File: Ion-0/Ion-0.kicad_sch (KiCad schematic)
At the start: 15 parts, among them J1 Beaglebone-green-P9, J2 Beaglebone-green-P8, J3 Conn_02x06_Odd_Even, J4 Conn_02x06_Odd_Even, J5 Conn_02x06_Odd_Even

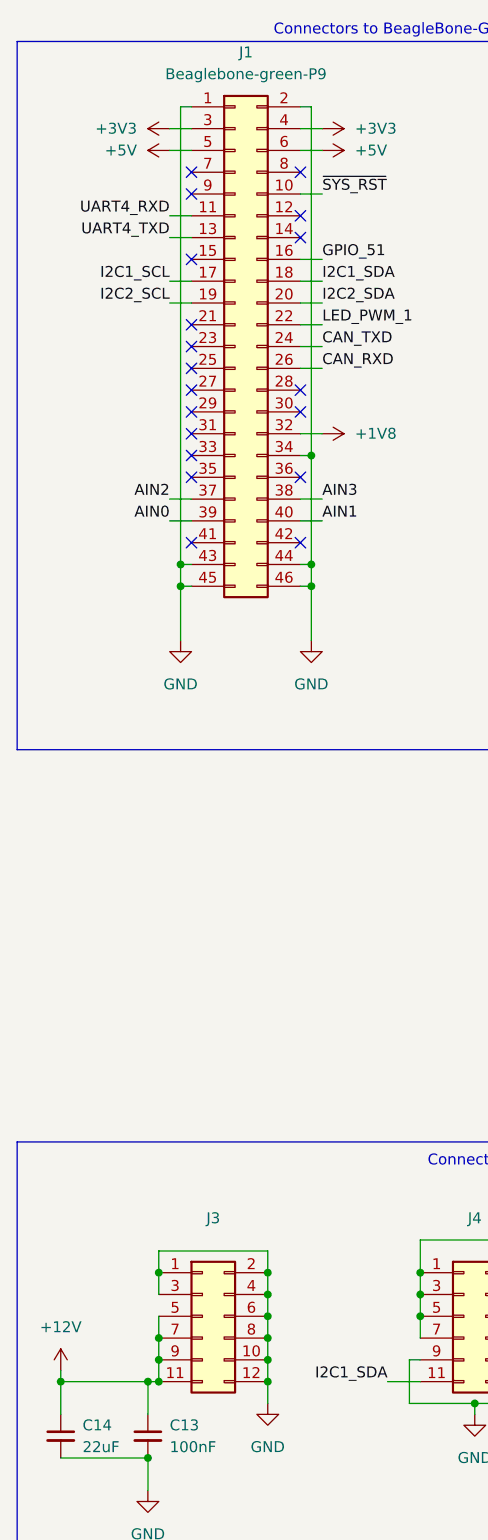
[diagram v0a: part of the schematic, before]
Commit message: Fixed symbol library
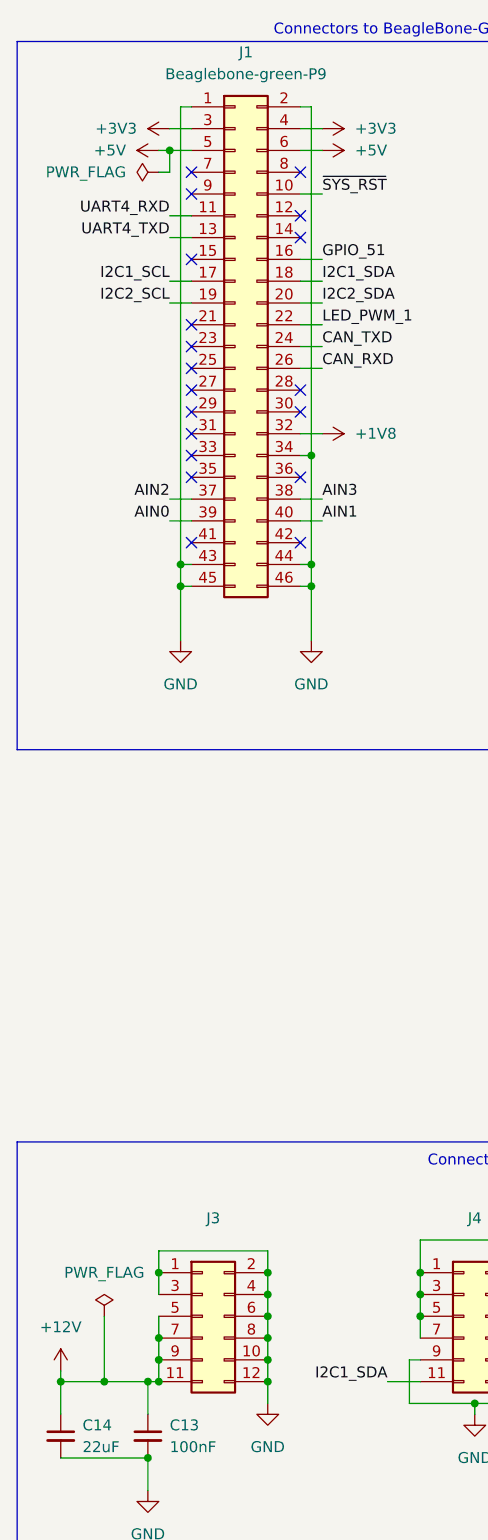
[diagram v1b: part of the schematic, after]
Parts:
- J1: footprint Connector_PinHeader_1.00mm:PinHeader_2x23_P1.00mm_Horizontal -> Connector_PinHeader_1.00mm:PinHeader_2x23_P1.00mm_Vertical
- J2: footprint (none) -> Connector_PinHeader_1.00mm:PinHeader_2x23_P1.00mm_Vertical
- J3, J4, J5: footprint (none) -> Connector_PinHeader_1.00mm:PinHeader_2x06_P1.00mm_Vertical

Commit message: library fix, no 3d models tho
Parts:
- C13, C14, C15, C16, C17, C18: footprint (none) -> Capacitor_SMD:C_0201_0603Metric
- J1, J2: footprint Connector_PinHeader_1.00mm:PinHeader_2x23_P1.00mm_Vertical -> Connector_PinHeader_2.54mm:PinHeader_2x23_P2.54mm_Vertical
- J3, J4, J5: footprint Connector_PinHeader_1.00mm:PinHeader_2x06_P1.00mm_Vertical -> Connector_PinSocket_2.54mm:PinSocket_2x06_P2.54mm_Vertical
- R19, R20, R6, R7: footprint (none) -> Resistor_SMD:R_0603_1608Metric_Pad0.98x0.95mm_HandSolder
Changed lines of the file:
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@@
 			)
 		)
-		(property "Footprint" "Connector_PinHeader_1.00mm:PinHeader_2x06_P1.00mm_Vertical"
+		(property "Footprint" "Connector_PinSocket_2.54mm:PinSocket_2x06_P2.54mm_Vertical"
 			(at 67.31 163.83 0)
 			(hide yes)
@@
 			)
 		)
-		(property "Footprint" ""
+		(property "Footprint" "Capacitor_SMD:C_0201_0603Metric"
 			(at 90.17 161.29 0)
 			(hide yes)
@@
 			)
 		)
-		(property "Footprint" ""
+		(property "Footprint" "Capacitor_SMD:C_0201_0603Metric"
 			(at 80.01 161.29 0)
 			(hide yes)
@@
 			)
 		)
-		(property "Footprint" ""
+		(property "Footprint" "Resistor_SMD:R_0603_1608Metric_Pad0.98x0.95mm_HandSolder"
 			(at 186.69 48.26 0)
 			(hide yes)
@@
 			)
 		)
-		(property "Footprint" "Connector_PinHeader_1.00mm:PinHeader_2x23_P1.00mm_Vertical"
+		(property "Footprint" "Connector_PinHeader_2.54mm:PinHeader_2x23_P2.54mm_Vertical"
 			(at 95.25 52.07 0)
 			(hide yes)
@@
 			)
 		)
-		(property "Footprint" ""
+		(property "Footprint" "Resistor_SMD:R_0603_1608Metric_Pad0.98x0.95mm_HandSolder"
 			(at 194.31 48.26 0)
 			(hide yes)
@@
 			)
 		)
-		(property "Footprint" "Connector_PinHeader_1.00mm:PinHeader_2x06_P1.00mm_Vertical"
+		(property "Footprint" "Connector_PinSocket_2.54mm:PinSocket_2x06_P2.54mm_Vertical"
 			(at 36.83 163.83 0)
 			(hide yes)
@@
 			)
 		)
-		(property "Footprint" ""
+		(property "Footprint" "Capacitor_SMD:C_0201_0603Metric"
 			(at 123.19 168.91 0)
 			(hide yes)
@@
 			)
 		)
-		(property "Footprint" "Connector_PinHeader_1.00mm:PinHeader_2x23_P1.00mm_Vertical"
+		(property "Footprint" "Connector_PinHeader_2.54mm:PinHeader_2x23_P2.54mm_Vertical"
 			(at 40.64 50.8 0)
 			(hide yes)
@@
 			)
 		)
-		(property "Footprint" ""
+		(property "Footprint" "Capacitor_SMD:C_0201_0603Metric"
 			(at 133.35 168.91 0)
 			(hide yes)
@@
 			)
 		)
-		(property "Footprint" ""
+		(property "Footprint" "Capacitor_SMD:C_0201_0603Metric"
 			(at 20.32 177.8 0)
 			(hide yes)
@@
 			)
 		)
-		(property "Footprint" ""
+		(property "Footprint" "Resistor_SMD:R_0603_1608Metric_Pad0.98x0.95mm_HandSolder"
 			(at 179.07 48.26 0)
 			(hide yes)
@@
 			)
 		)
-		(property "Footprint" ""
+		(property "Footprint" "Resistor_SMD:R_0603_1608Metric_Pad0.98x0.95mm_HandSolder"
 			(at 171.45 48.26 0)
 			(hide yes)
@@
 			)
 		)
-		(property "Footprint" ""
+		(property "Footprint" "Capacitor_SMD:C_0201_0603Metric"
 			(at 30.48 177.8 0)
 			(hide yes)
@@
 			)
 		)
-		(property "Footprint" "Connector_PinHeader_1.00mm:PinHeader_2x06_P1.00mm_Vertical"
+		(property "Footprint" "Connector_PinSocket_2.54mm:PinSocket_2x06_P2.54mm_Vertical"
 			(at 147.32 163.83 0)
 			(hide yes)
